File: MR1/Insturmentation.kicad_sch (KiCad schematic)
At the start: 10 parts, among them J7 Conn_01x14_MountingPin

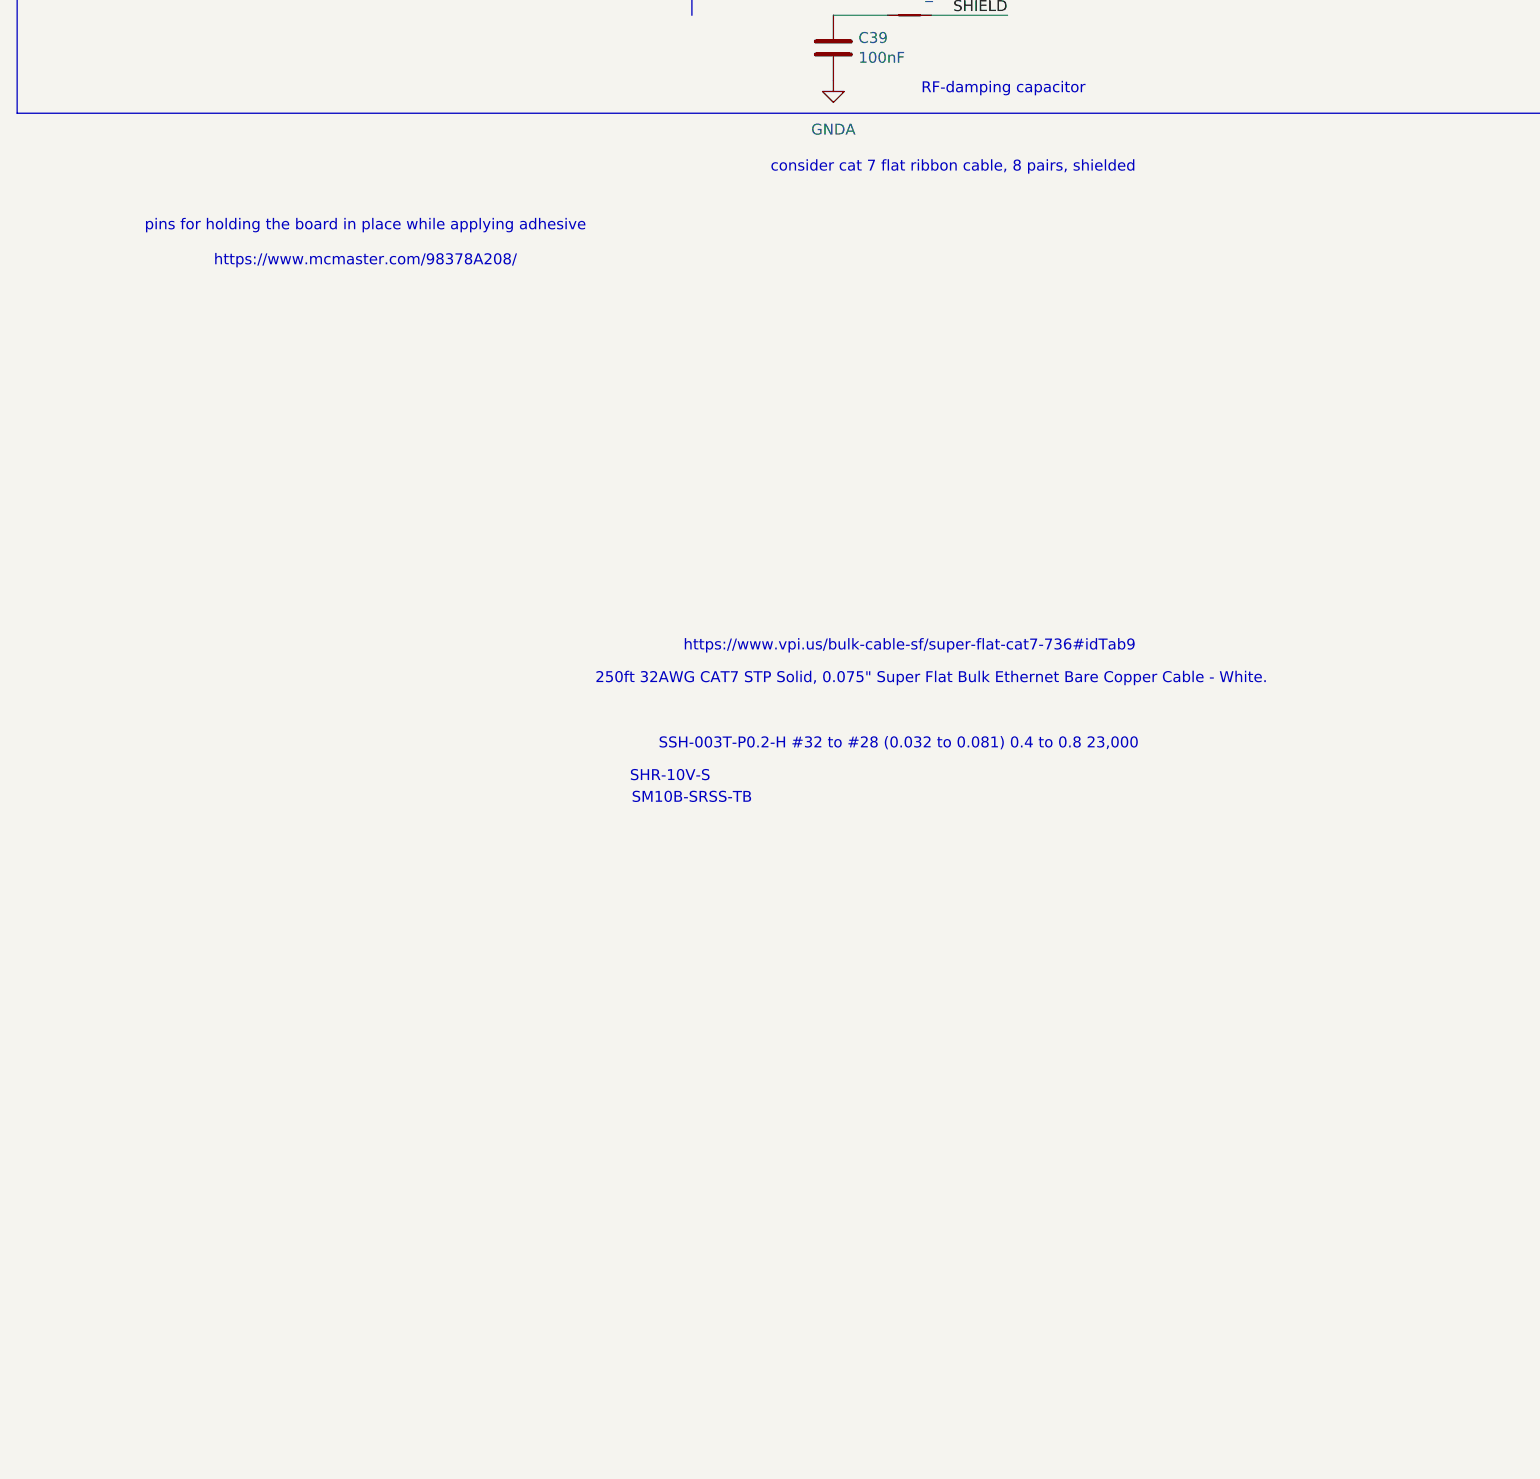
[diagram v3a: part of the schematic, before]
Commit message: chore: prepare repository and documentation for open-source release
- Removed internal .agents scaffolding and updated .gitignore
- Added CONTRIBUTING.md with CAD, PCB, firmware, and PR guidelines
- Added CODE_OF_CONDUCT.md (Contributor Covenant v2.1)
- Added SECURITY.md with hardware safety and vulnerability disclosure policies
- Added CITATION.cff for academic and scientific publications
- Added Pump_firmware/README.md for STM32G431 subsystem
- Expanded BOM.md with mechanical, fluidic, PCB, and active electronics
- Updated README.md test badges, architecture, and documentation index
- Cleared hardcoded absolute developer paths in export_manager.py and KiCad files
- Fixed formatting in install.sh and metadata in package.json
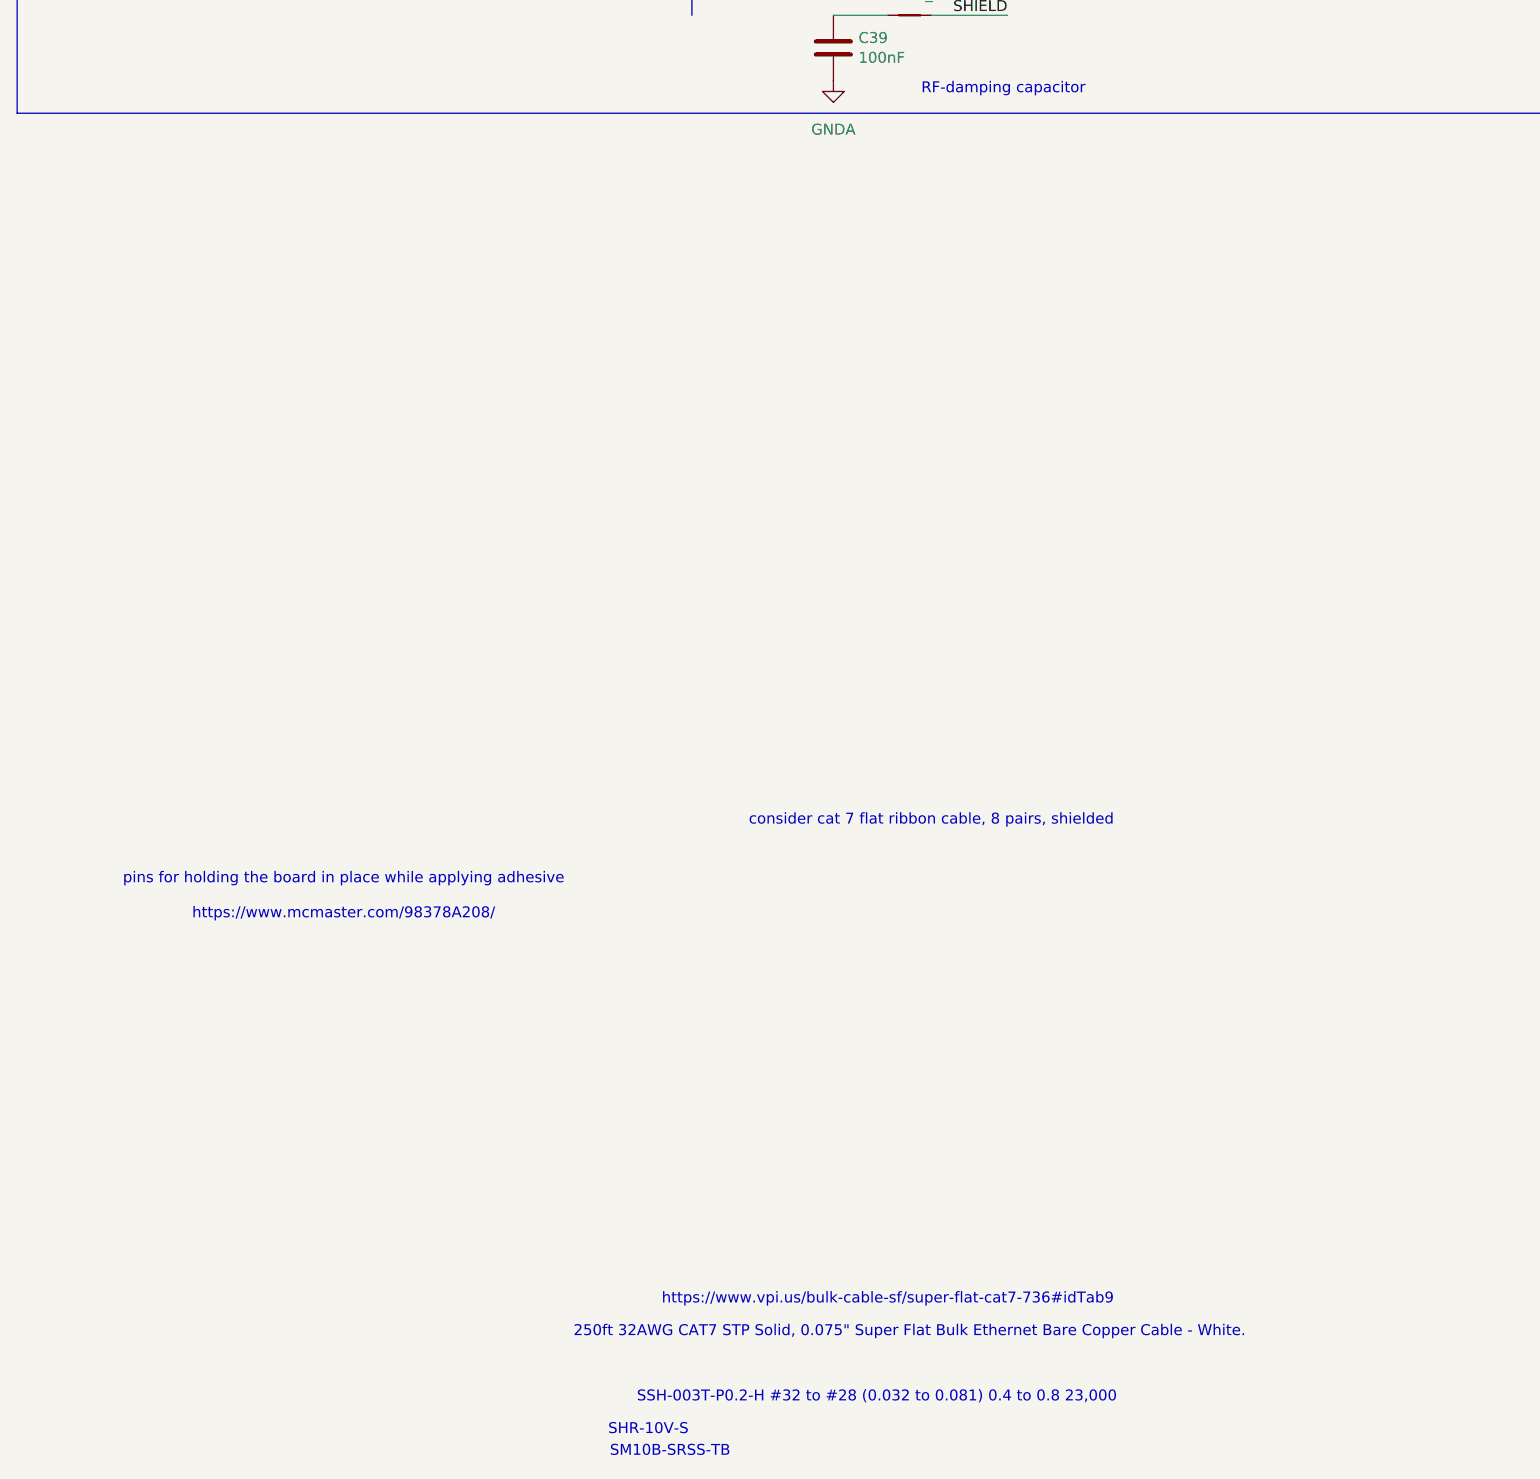
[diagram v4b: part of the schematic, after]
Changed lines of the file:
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@@
 	(text "consider cat 7 flat ribbon cable, 8 pairs, shielded"
 		(exclude_from_sim no)
-		(at 124.46 142.24 0)
+		(at 121.92 218.44 0)
 		(effects
 			(font
@@
 	(text "pins for holding the board in place while applying adhesive\n\nhttps://www.mcmaster.com/98378A208/"
 		(exclude_from_sim no)
-		(at 55.88 151.13 0)
+		(at 53.34 227.33 0)
 		(effects
 			(font
@@
 	(text "https://www.vpi.us/bulk-cable-sf/super-flat-cat7-736#idTab9"
 		(exclude_from_sim no)
-		(at 119.38 198.12 0)
+		(at 116.84 274.32 0)
 		(effects
 			(font
@@
 	(text "SM10B-SRSS-TB"
 		(exclude_from_sim no)
-		(at 93.98 215.9 0)
+		(at 91.44 292.1 0)
 		(effects
 			(font
@@
 	(text "250ft 32AWG CAT7 STP Solid, 0.075\" Super Flat Bulk Ethernet Bare Copper Cable - White."
 		(exclude_from_sim no)
-		(at 121.92 201.93 0)
+		(at 119.38 278.13 0)
 		(effects
 			(font
@@
 	(text "SHR-10V-S"
 		(exclude_from_sim no)
-		(at 91.44 213.36 0)
+		(at 88.9 289.56 0)
 		(effects
 			(font
@@
 	(text "SSH-003T-P0.2-H #32 to #28 (0.032 to 0.081) 0.4 to 0.8 23,000\n"
 		(exclude_from_sim no)
-		(at 118.11 209.55 0)
+		(at 115.57 285.75 0)
 		(effects
 			(font
@@
 	)
 	(image
-		(at 121.92 184.15)
+		(at 119.38 260.35)
 		(data "iVBORw0KGgoAAAANSUhEUgAAAm8AAADlCAYAAAAFghAfAAAABHNCSVQICAgIfAhkiAAAIABJREFU"
 			"eJzsfXmUXFW1/ldVt+apx3SS7swd0gkJCUHGBEGmBBIMPoTHAgQZRBAez7d+iBKXiiiKDxHx4Vuo"
@@
 	)
 	(image
-		(at 123.19 160.02)
+		(at 120.65 236.22)
 		(scale 3.20589)
 		(data "iVBORw0KGgoAAAANSUhEUgAAAFoAAABaCAYAAAA4qEECAAAABHNCSVQICAgIfAhkiAAADmNJREFU"
